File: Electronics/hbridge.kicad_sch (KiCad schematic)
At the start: 37 parts, among them Q201 IRLZ44N, Q202 IRLIZ44N, Q203 IRLZ44N, Q204 IRLIZ44N, Q205 IRLZ44N, Q206 IRLIZ44N, U201 74LS08, U202 IR2101, U203 IR2101, U204 IR2101

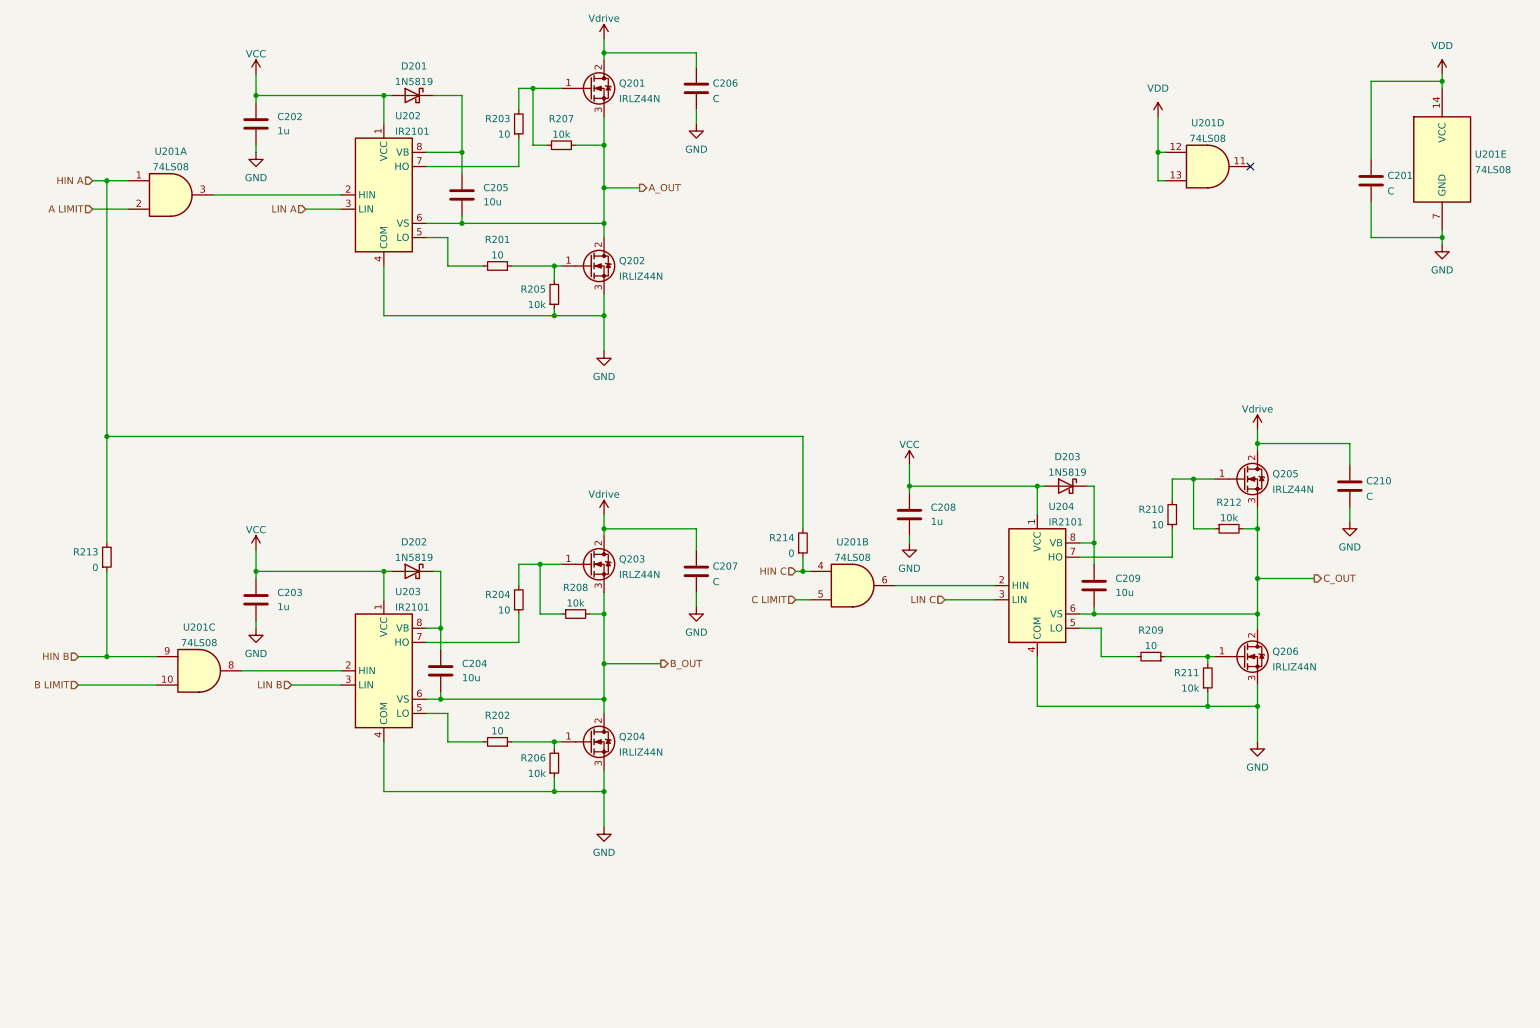
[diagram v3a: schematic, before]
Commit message: Added Current sensor finalized layout version 0.1
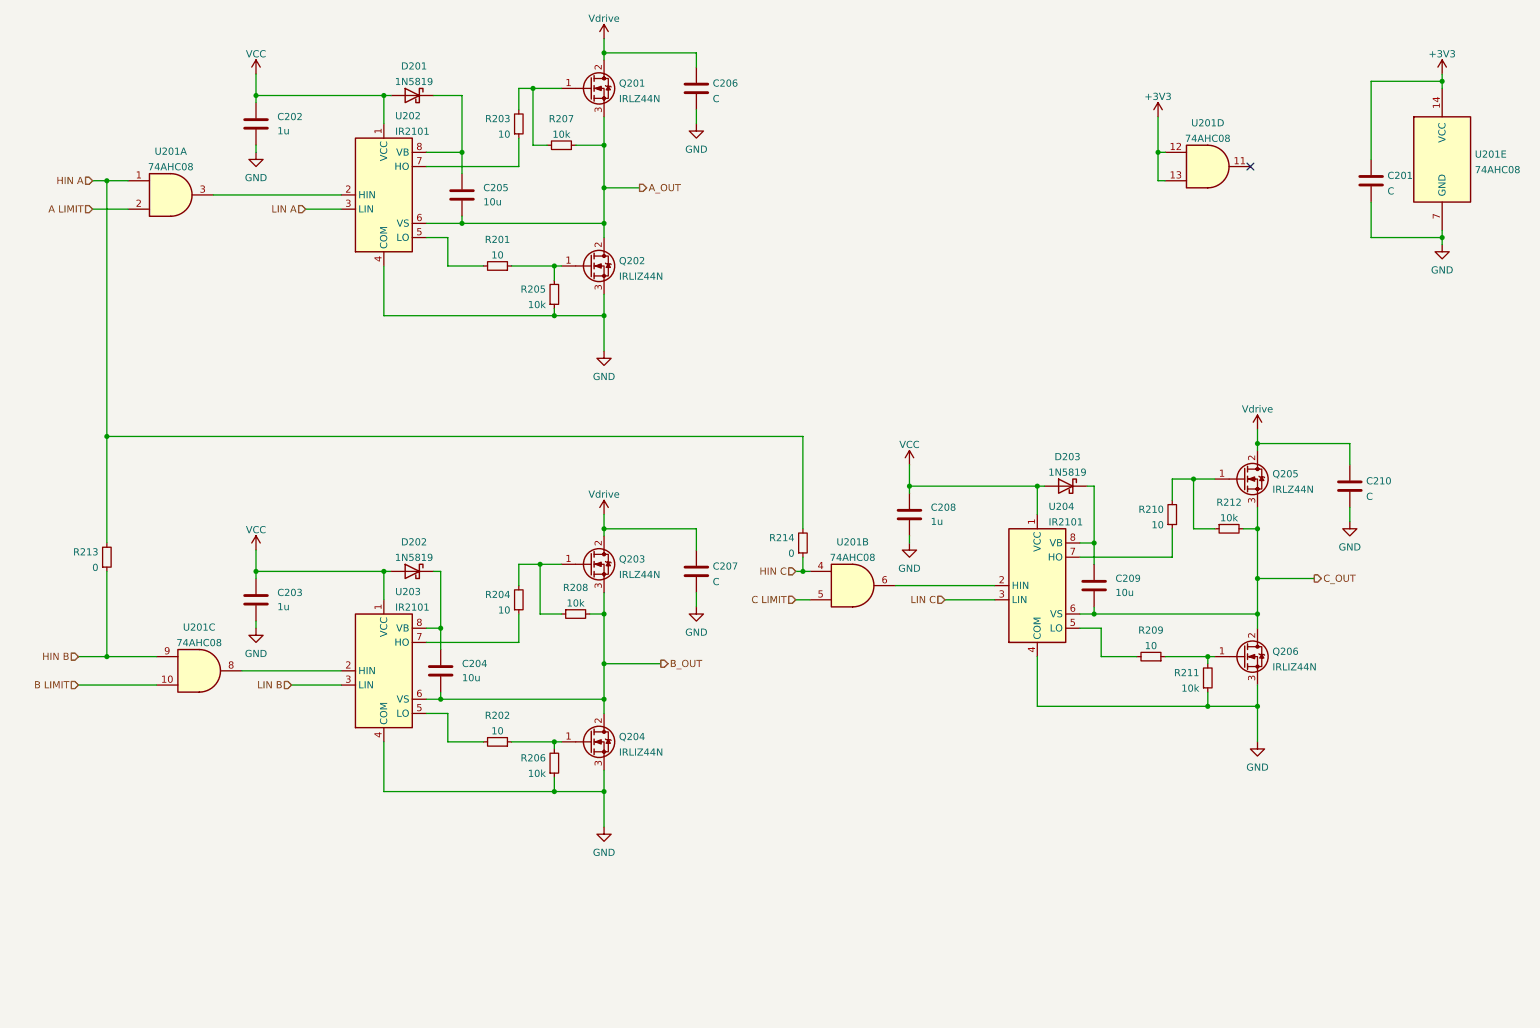
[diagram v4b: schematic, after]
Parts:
- C204, C205, C209: footprint Capacitor_SMD:C_0603_1608Metric_Pad1.08x0.95mm_HandSolder -> Resistor_SMD:R_0805_2012Metric_Pad1.20x1.40mm_HandSolder
- R213, R214: footprint Resistor_SMD:R_0805_2012Metric_Pad1.20x1.40mm_HandSolder -> Resistor_SMD:R_0603_1608Metric_Pad0.98x0.95mm_HandSolder
- U201: value 74LS08 -> 74AHC08
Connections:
- net VDD renamed +3V3
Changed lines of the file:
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@@
       (effects (font (size 1.27 1.27)) (justify right))
     )
-    (property "Footprint" "Capacitor_SMD:C_0603_1608Metric_Pad1.08x0.95mm_HandSolder" (id 2) (at 86.6648 127 0)
+    (property "Footprint" "Resistor_SMD:R_0805_2012Metric_Pad1.20x1.40mm_HandSolder" (id 2) (at 86.6648 127 0)
       (effects (font (size 1.27 1.27)) hide)
     )
@@
       (effects (font (size 1.27 1.27)) (justify right))
     )
-    (property "Footprint" "Resistor_SMD:R_0805_2012Metric_Pad1.20x1.40mm_HandSolder" (id 2) (at 27.94 110.49 0)
+    (property "Footprint" "Resistor_SMD:R_0603_1608Metric_Pad0.98x0.95mm_HandSolder" (id 2) (at 27.94 110.49 0)
       (effects (font (size 1.27 1.27)) hide)
     )
@@
     (in_bom yes) (on_board yes) (fields_autoplaced)
     (property "Reference" "U201" (id 0) (at 161.29 107.7935 0))
-    (property "Value" "74LS08" (id 1) (at 161.29 110.5686 0))
+    (property "Value" "74AHC08" (id 1) (at 161.29 110.5686 0))
     (property "Footprint" "Package_SO:SO-14_3.9x8.65mm_P1.27mm" (id 2) (at 161.29 115.57 0)
       (effects (font (size 1.27 1.27)) hide)
@@
       (effects (font (size 1.27 1.27)) (justify right))
     )
-    (property "Footprint" "Capacitor_SMD:C_0603_1608Metric_Pad1.08x0.95mm_HandSolder" (id 2) (at 203.5048 111.76 0)
+    (property "Footprint" "Resistor_SMD:R_0805_2012Metric_Pad1.20x1.40mm_HandSolder" (id 2) (at 203.5048 111.76 0)
       (effects (font (size 1.27 1.27)) hide)
     )
@@
       (effects (font (size 1.27 1.27)) (justify right))
     )
-    (property "Footprint" "Resistor_SMD:R_0805_2012Metric_Pad1.20x1.40mm_HandSolder" (id 2) (at 152.4 107.95 0)
+    (property "Footprint" "Resistor_SMD:R_0603_1608Metric_Pad0.98x0.95mm_HandSolder" (id 2) (at 152.4 107.95 0)
       (effects (font (size 1.27 1.27)) hide)
     )
@@
       (effects (font (size 1.27 1.27)) (justify right))
     )
-    (property "Footprint" "Capacitor_SMD:C_0603_1608Metric_Pad1.08x0.95mm_HandSolder" (id 2) (at 90.4748 41.91 0)
+    (property "Footprint" "Resistor_SMD:R_0805_2012Metric_Pad1.20x1.40mm_HandSolder" (id 2) (at 90.4748 41.91 0)
       (effects (font (size 1.27 1.27)) hide)
     )
@@
     (in_bom yes) (on_board yes) (fields_autoplaced)
     (property "Reference" "U201" (id 0) (at 44.45 123.0335 0))
-    (property "Value" "74LS08" (id 1) (at 44.45 125.8086 0))
+    (property "Value" "74AHC08" (id 1) (at 44.45 125.8086 0))
     (property "Footprint" "Package_SO:SO-14_3.9x8.65mm_P1.27mm" (id 2) (at 44.45 130.81 0)
       (effects (font (size 1.27 1.27)) hide)
@@
     (pin "2")
   )
-  (symbol (lib_id "power:VDD") (at 266.7 24.13 0) (unit 1)
-    (in_bom yes) (on_board yes) (fields_autoplaced)
-    (property "Reference" "#PWR0109" (id 0) (at 266.7 27.94 0)
-      (effects (font (size 1.27 1.27)) hide)
-    )
-    (property "Value" "VDD" (id 1) (at 266.7 19.05 0))
-    (property "Footprint" "" (id 2) (at 266.7 24.13 0)
-      (effects (font (size 1.27 1.27)) hide)
-    )
-    (property "Datasheet" "" (id 3) (at 266.7 24.13 0)
-      (effects (font (size 1.27 1.27)) hide)
-    )
-    (pin "1")
-  )
   (symbol (lib_id "power:GND") (at 133.35 119.38 0) (unit 1)
     (in_bom yes) (on_board yes) (fields_autoplaced)
@@
       (effects (font (size 1.27 1.27)) (justify left))
     )
-    (property "Value" "74LS08" (id 1) (at 272.542 41.2366 0)
+    (property "Value" "74AHC08" (id 1) (at 272.542 41.2366 0)
       (effects (font (size 1.27 1.27)) (justify left))
     )
@@
     (pin "2")
   )
-  (symbol (lib_id "power:VDD") (at 215.9 31.75 0) (unit 1)
-    (in_bom yes) (on_board yes) (fields_autoplaced)
-    (property "Reference" "#PWR0111" (id 0) (at 215.9 35.56 0)
-      (effects (font (size 1.27 1.27)) hide)
-    )
-    (property "Value" "VDD" (id 1) (at 215.9 26.67 0))
-    (property "Footprint" "" (id 2) (at 215.9 31.75 0)
-      (effects (font (size 1.27 1.27)) hide)
-    )
-    (property "Datasheet" "" (id 3) (at 215.9 31.75 0)
-      (effects (font (size 1.27 1.27)) hide)
-    )
-    (pin "1")
-  )
   (symbol (lib_id "Device:R_Small") (at 101.6 33.02 0) (mirror x) (unit 1)
     (in_bom yes) (on_board yes) (fields_autoplaced)
@@
     (in_bom yes) (on_board yes) (fields_autoplaced)
     (property "Reference" "U201" (id 0) (at 224.79 32.8635 0))
-    (property "Value" "74LS08" (id 1) (at 224.79 35.6386 0))
+    (property "Value" "74AHC08" (id 1) (at 224.79 35.6386 0))
     (property "Footprint" "Package_SO:SO-14_3.9x8.65mm_P1.27mm" (id 2) (at 224.79 40.64 0)
       (effects (font (size 1.27 1.27)) hide)
@@
     (pin "1")
   )
+  (symbol (lib_id "power:+3V3") (at 215.9 31.75 0) (unit 1)
+    (in_bom yes) (on_board yes) (fields_autoplaced)
+    (property "Reference" "#PWR0109" (id 0) (at 215.9 35.56 0)
+      (effects (font (size 1.27 1.27)) hide)
+    )
+    (property "Value" "+3V3" (id 1) (at 215.9 28.1455 0))
+    (property "Footprint" "" (id 2) (at 215.9 31.75 0)
+      (effects (font (size 1.27 1.27)) hide)
+    )
+    (property "Datasheet" "" (id 3) (at 215.9 31.75 0)
+      (effects (font (size 1.27 1.27)) hide)
+    )
+    (pin "1")
+  )
   (symbol (lib_id "Device:R_Small") (at 101.6 118.11 0) (mirror x) (unit 1)
     (in_bom yes) (on_board yes) (fields_autoplaced)
@@
     (pin "2")
   )
+  (symbol (lib_id "power:+3V3") (at 266.7 24.13 0) (unit 1)
+    (in_bom yes) (on_board yes) (fields_autoplaced)
+    (property "Reference" "#PWR0111" (id 0) (at 266.7 27.94 0)
+      (effects (font (size 1.27 1.27)) hide)
+    )
+    (property "Value" "+3V3" (id 1) (at 266.7 20.5255 0))
+    (property "Footprint" "" (id 2) (at 266.7 24.13 0)
+      (effects (font (size 1.27 1.27)) hide)
+    )
+    (property "Datasheet" "" (id 3) (at 266.7 24.13 0)
+      (effects (font (size 1.27 1.27)) hide)
+    )
+    (pin "1")
+  )
   (symbol (lib_id "Device:C") (at 54.61 118.11 180) (unit 1)
     (in_bom yes) (on_board yes) (fields_autoplaced)
@@
     (in_bom yes) (on_board yes) (fields_autoplaced)
     (property "Reference" "U201" (id 0) (at 39.37 37.9435 0))
-    (property "Value" "74LS08" (id 1) (at 39.37 40.7186 0))
+    (property "Value" "74AHC08" (id 1) (at 39.37 40.7186 0))
     (property "Footprint" "Package_SO:SO-14_3.9x8.65mm_P1.27mm" (id 2) (at 39.37 45.72 0)
       (effects (font (size 1.27 1.27)) hide)

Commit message: Chaned 74AHC08 footprint to ssop-14
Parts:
- U201: footprint Package_SO:SO-14_3.9x8.65mm_P1.27mm -> Package_SO:SSOP-14_5.3x6.2mm_P0.65mm
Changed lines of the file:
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@@
     (property "Reference" "U201" (id 0) (at 161.29 107.7935 0))
     (property "Value" "74AHC08" (id 1) (at 161.29 110.5686 0))
-    (property "Footprint" "Package_SO:SO-14_3.9x8.65mm_P1.27mm" (id 2) (at 161.29 115.57 0)
+    (property "Footprint" "Package_SO:SSOP-14_5.3x6.2mm_P0.65mm" (id 2) (at 161.29 115.57 0)
       (effects (font (size 1.27 1.27)) hide)
     )
@@
     (property "Reference" "U201" (id 0) (at 44.45 123.0335 0))
     (property "Value" "74AHC08" (id 1) (at 44.45 125.8086 0))
-    (property "Footprint" "Package_SO:SO-14_3.9x8.65mm_P1.27mm" (id 2) (at 44.45 130.81 0)
+    (property "Footprint" "Package_SO:SSOP-14_5.3x6.2mm_P0.65mm" (id 2) (at 44.45 130.81 0)
       (effects (font (size 1.27 1.27)) hide)
     )
@@
       (effects (font (size 1.27 1.27)) (justify left))
     )
-    (property "Footprint" "Package_SO:SO-14_3.9x8.65mm_P1.27mm" (id 2) (at 266.7 39.37 0)
+    (property "Footprint" "Package_SO:SSOP-14_5.3x6.2mm_P0.65mm" (id 2) (at 266.7 39.37 0)
       (effects (font (size 1.27 1.27)) hide)
     )
@@
     (property "Reference" "U201" (id 0) (at 224.79 32.8635 0))
     (property "Value" "74AHC08" (id 1) (at 224.79 35.6386 0))
-    (property "Footprint" "Package_SO:SO-14_3.9x8.65mm_P1.27mm" (id 2) (at 224.79 40.64 0)
+    (property "Footprint" "Package_SO:SSOP-14_5.3x6.2mm_P0.65mm" (id 2) (at 224.79 40.64 0)
       (effects (font (size 1.27 1.27)) hide)
     )
@@
     (property "Reference" "U201" (id 0) (at 39.37 37.9435 0))
     (property "Value" "74AHC08" (id 1) (at 39.37 40.7186 0))
-    (property "Footprint" "Package_SO:SO-14_3.9x8.65mm_P1.27mm" (id 2) (at 39.37 45.72 0)
-      (effects (font (size 1.27 1.27)) hide)
-    )
+    (property "Footprint" "Package_SO:SSOP-14_5.3x6.2mm_P0.65mm" (id 2) (at 39.37 45.72 0)
+      (effects (font (size 1.27 1.27)) hide)
+    )
